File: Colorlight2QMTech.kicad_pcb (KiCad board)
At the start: 4 copper layers, 66 x 85.7 mm, 18 parts, among them CN1 1473005-4, J1 Conn_02x32_Odd_Even, J2 Conn_02x32_Odd_Even, J3 Connector_USB_C_Receptacle_US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, J4 Conn_01x14_Male, J4-GND1 Conn_01x01_Male, J5 Conn_01x14_Male, U1 AMS1117-3.3

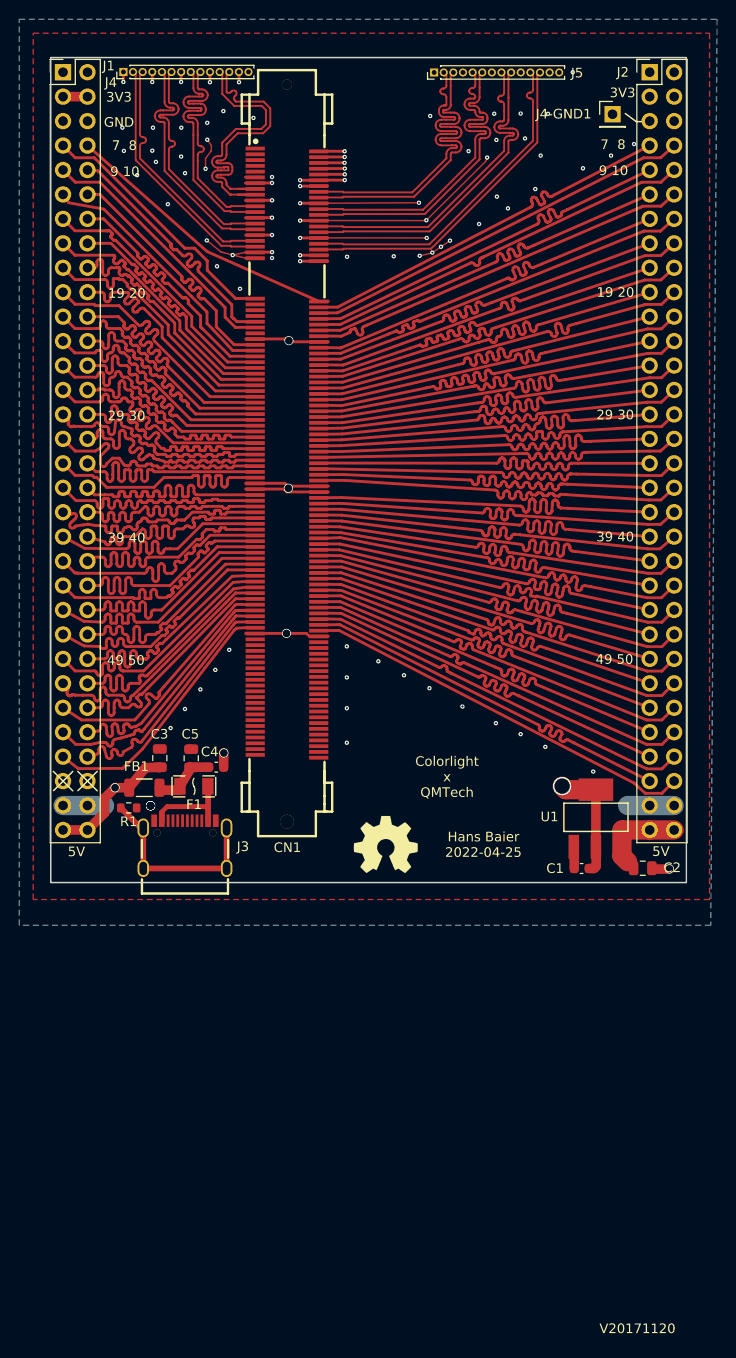
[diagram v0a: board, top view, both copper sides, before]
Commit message: make track widths a bit smaller to satisfy .105mm spacing
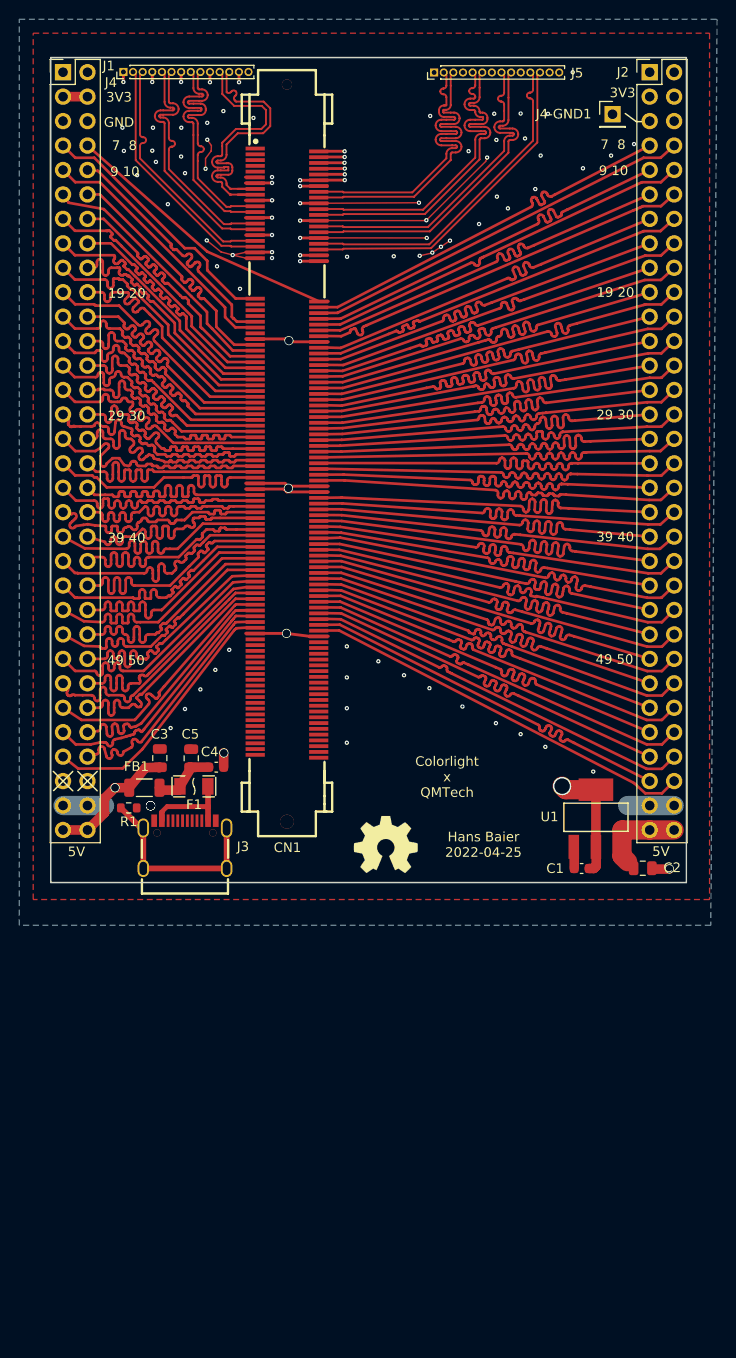
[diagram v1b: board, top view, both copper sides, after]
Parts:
- removed N2: V20171120, SquantorLabels:Label_version
